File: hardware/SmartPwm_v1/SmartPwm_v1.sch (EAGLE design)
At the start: 41 parts, among them IC1 7805T, J1 ESP32-PICO-KIT, Q1 IRF3704-H, Q2 IRF3704-H, Q3 IRF3704-H, Q4 IRF3704-H, U1 ICL7667CBAZA, U3 ICL7667CBAZA

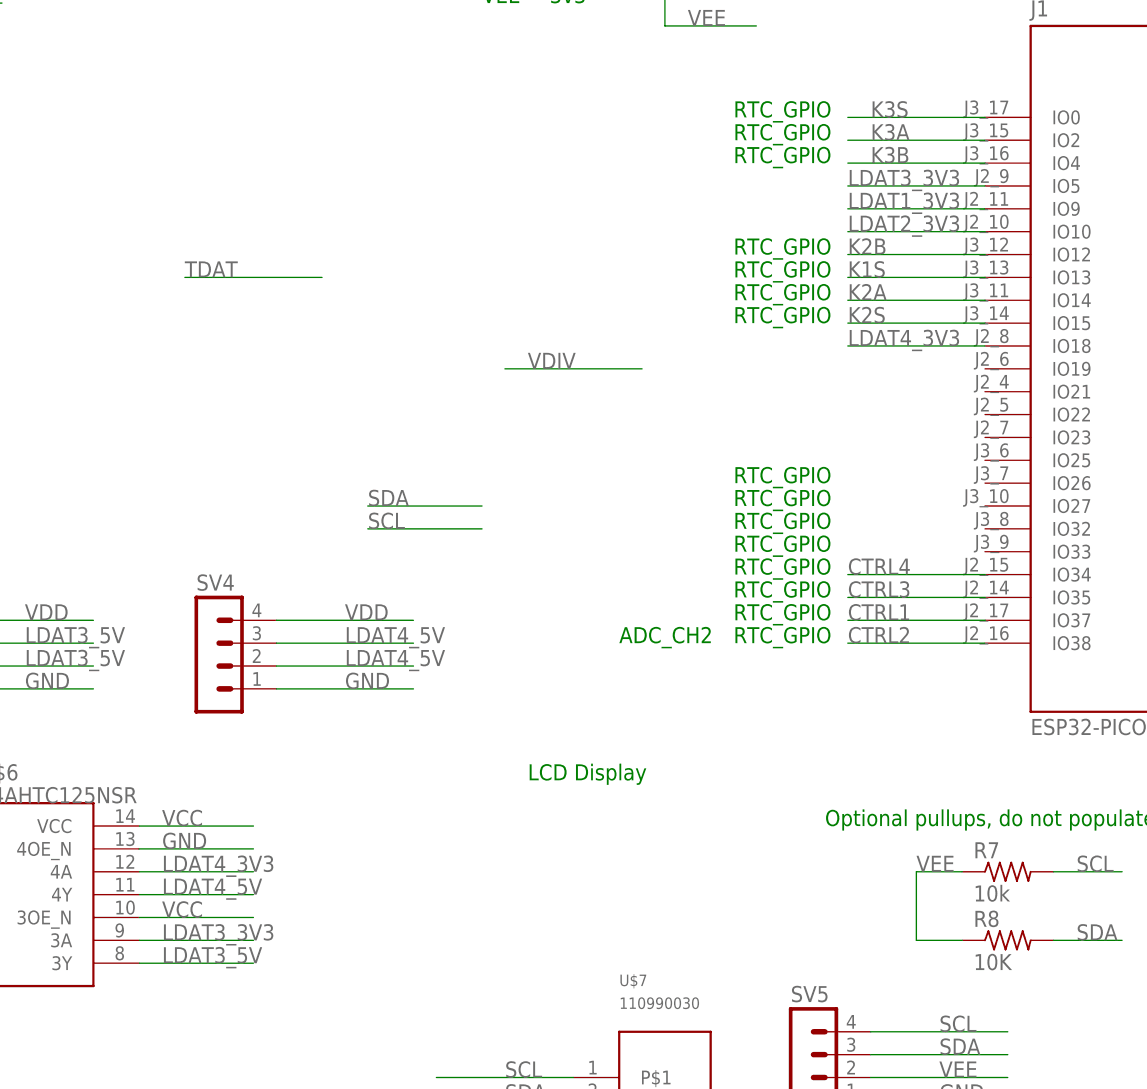
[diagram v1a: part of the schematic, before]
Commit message: did routing, but need to fix ctrl pins, since they were routed to inputs on the pico kit...
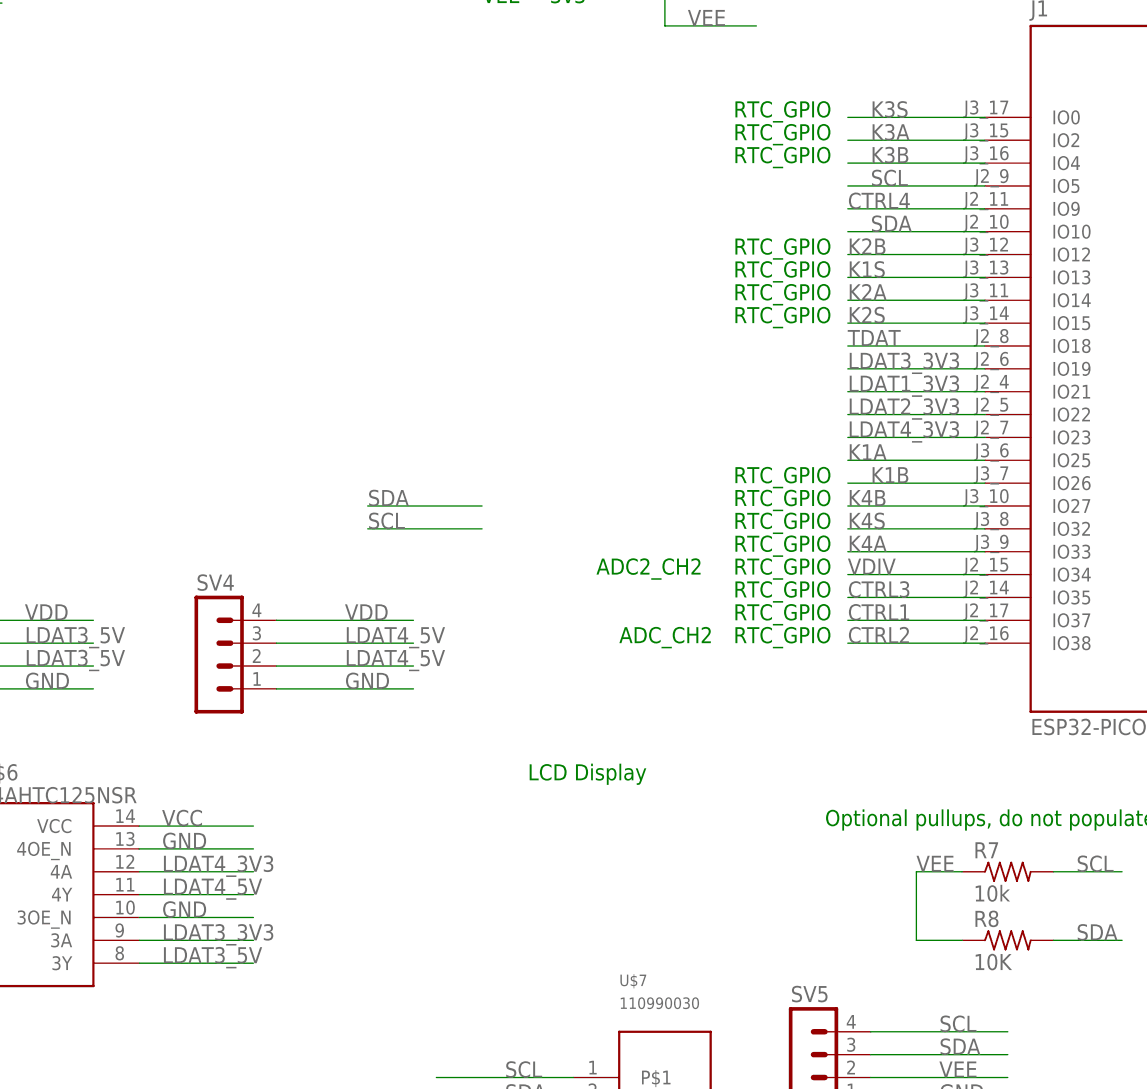
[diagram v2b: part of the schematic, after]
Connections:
- net CTRL4: now also J1.IO9; no longer J1.IO34
- net GND: now also U$6.3OE_N
- net K1A: now also J1.IO25
- net K1B: now also J1.IO26
- net K4A: now also J1.IO33
- net K4B: now also J1.IO27
- net K4S: now also J1.IO32
- net LDAT1_3V3: now also J1.IO21; no longer J1.IO9
- net LDAT2_3V3: now also J1.IO22; no longer J1.IO10
- net LDAT3_3V3: now also J1.IO19; no longer J1.IO5
- net LDAT4_3V3: now also J1.IO23; no longer J1.IO18
- net SCL: now also J1.IO5
- net SDA: now also J1.IO10
- net TDAT: now also J1.IO18
- net VCC: no longer U$6.3OE_N
- net VDIV: now also J1.IO34
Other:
- note added: "ADC2_CH2"
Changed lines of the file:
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@@
 <text x="228.6" y="-58.42" size="1.778" layer="91">tantalum</text>
 <text x="266.7" y="-58.42" size="1.778" layer="91">lowimpedance</text>
+<text x="7.62" y="-38.1" size="1.778" layer="91">ADC2_CH2</text>
 </plain>
 <instances>
@@
 <pinref part="SV4" gate="1" pin="1"/>
 </segment>
+<segment>
+<wire x1="-30.48" y1="-76.2" x2="-43.18" y2="-76.2" width="0.1524" layer="91"/>
+<label x="-40.64" y="-76.2" size="1.778" layer="95"/>
+<pinref part="U$6" gate="G$1" pin="3OE_N"/>
+</segment>
 </net>
 <net name="VCC" class="0">
@@
 <label x="-40.64" y="-66.04" size="1.778" layer="95"/>
 <pinref part="U$6" gate="G$1" pin="VCC"/>
-</segment>
-<segment>
-<wire x1="-30.48" y1="-76.2" x2="-43.18" y2="-76.2" width="0.1524" layer="91"/>
-<label x="-40.64" y="-76.2" size="1.778" layer="95"/>
-<pinref part="U$6" gate="G$1" pin="3OE_N"/>
 </segment>
 </net>
@@
 </segment>
 <segment>
-<wire x1="50.8" y1="-38.1" x2="35.56" y2="-38.1" width="0.1524" layer="91"/>
-<label x="35.56" y="-38.1" size="1.778" layer="95"/>
-<pinref part="J1" gate="G$1" pin="IO34"/>
+<wire x1="50.8" y1="2.54" x2="35.56" y2="2.54" width="0.1524" layer="91"/>
+<label x="35.56" y="2.54" size="1.778" layer="95"/>
+<pinref part="J1" gate="G$1" pin="IO9"/>
 </segment>
 </net>
@@
 <label x="-17.78" y="-33.02" size="1.778" layer="95"/>
 </segment>
+<segment>
+<wire x1="50.8" y1="5.08" x2="35.56" y2="5.08" width="0.1524" layer="91"/>
+<label x="38.1" y="5.08" size="1.778" layer="95"/>
+<pinref part="J1" gate="G$1" pin="IO5"/>
+</segment>
 </net>
 <net name="SDA" class="0">
@@
 <wire x1="-5.08" y1="-30.48" x2="-17.78" y2="-30.48" width="0.1524" layer="91"/>
 <label x="-17.78" y="-30.48" size="1.778" layer="95"/>
+</segment>
+<segment>
+<wire x1="50.8" y1="0" x2="35.56" y2="0" width="0.1524" layer="91"/>
+<label x="38.1" y="0" size="1.778" layer="95"/>
+<pinref part="J1" gate="G$1" pin="IO10"/>
 </segment>
 </net>
@@
 </segment>
 <segment>
-<wire x1="-22.86" y1="-5.08" x2="-38.1" y2="-5.08" width="0.1524" layer="91"/>
-<label x="-38.1" y="-5.08" size="1.778" layer="95"/>
+<wire x1="50.8" y1="-12.7" x2="35.56" y2="-12.7" width="0.1524" layer="91"/>
+<label x="35.56" y="-12.7" size="1.778" layer="95"/>
+<pinref part="J1" gate="G$1" pin="IO18"/>
 </segment>
 </net>
@@
 <label x="-71.12" y="104.14" size="1.778" layer="95"/>
 </segment>
+<segment>
+<wire x1="50.8" y1="-27.94" x2="35.56" y2="-27.94" width="0.1524" layer="91"/>
+<label x="38.1" y="-27.94" size="1.778" layer="95"/>
+<pinref part="J1" gate="G$1" pin="IO26"/>
+</segment>
 </net>
 <net name="K4S" class="0">
@@
 <pinref part="MT4" gate="G$1" pin="2"/>
 </segment>
+<segment>
+<wire x1="50.8" y1="-33.02" x2="35.56" y2="-33.02" width="0.1524" layer="91"/>
+<label x="35.56" y="-33.02" size="1.778" layer="95"/>
+<pinref part="J1" gate="G$1" pin="IO32"/>
+</segment>
 </net>
 <net name="K4A" class="0">
@@
 <pinref part="MT4" gate="G$1" pin="A"/>
 </segment>
+<segment>
+<pinref part="J1" gate="G$1" pin="IO33"/>
+<wire x1="50.8" y1="-35.56" x2="35.56" y2="-35.56" width="0.1524" layer="91"/>
+<label x="35.56" y="-35.56" size="1.778" layer="95"/>
+</segment>
 </net>
 <net name="K4B" class="0">
@@
 <label x="-71.12" y="25.4" size="1.778" layer="95"/>
 <pinref part="MT4" gate="G$1" pin="B"/>
+</segment>
+<segment>
+<wire x1="50.8" y1="-30.48" x2="35.56" y2="-30.48" width="0.1524" layer="91"/>
+<label x="35.56" y="-30.48" size="1.778" layer="95"/>
+<pinref part="J1" gate="G$1" pin="IO27"/>
 </segment>
 </net>
@@
 </segment>
 <segment>
-<wire x1="12.7" y1="-15.24" x2="-2.54" y2="-15.24" width="0.1524" layer="91"/>
-<label x="0" y="-15.24" size="1.778" layer="95"/>
+<wire x1="50.8" y1="-38.1" x2="35.56" y2="-38.1" width="0.1524" layer="91"/>
+<label x="35.56" y="-38.1" size="1.778" layer="95"/>
+<pinref part="J1" gate="G$1" pin="IO34"/>
 </segment>
 </net>
@@
 </segment>
 <segment>
-<wire x1="50.8" y1="2.54" x2="35.56" y2="2.54" width="0.1524" layer="91"/>
-<label x="35.56" y="2.54" size="1.778" layer="95"/>
-<pinref part="J1" gate="G$1" pin="IO9"/>
+<wire x1="50.8" y1="-17.78" x2="35.56" y2="-17.78" width="0.1524" layer="91"/>
+<label x="35.56" y="-17.78" size="1.778" layer="95"/>
+<pinref part="J1" gate="G$1" pin="IO21"/>
 </segment>
 </net>
@@
 </segment>
 <segment>
-<wire x1="50.8" y1="0" x2="35.56" y2="0" width="0.1524" layer="91"/>
-<label x="35.56" y="0" size="1.778" layer="95"/>
-<pinref part="J1" gate="G$1" pin="IO10"/>
+<wire x1="50.8" y1="-20.32" x2="35.56" y2="-20.32" width="0.1524" layer="91"/>
+<label x="35.56" y="-20.32" size="1.778" layer="95"/>
+<pinref part="J1" gate="G$1" pin="IO22"/>
 </segment>
 </net>
@@
 </segment>
 <segment>
-<wire x1="50.8" y1="-12.7" x2="35.56" y2="-12.7" width="0.1524" layer="91"/>
-<label x="35.56" y="-12.7" size="1.778" layer="95"/>
-<pinref part="J1" gate="G$1" pin="IO18"/>
+<wire x1="50.8" y1="-22.86" x2="35.56" y2="-22.86" width="0.1524" layer="91"/>
+<label x="35.56" y="-22.86" size="1.778" layer="95"/>
+<pinref part="J1" gate="G$1" pin="IO23"/>
 </segment>
 </net>
@@
 </segment>
 <segment>
-<wire x1="50.8" y1="5.08" x2="35.56" y2="5.08" width="0.1524" layer="91"/>
-<label x="35.56" y="5.08" size="1.778" layer="95"/>
-<pinref part="J1" gate="G$1" pin="IO5"/>
+<wire x1="50.8" y1="-15.24" x2="35.56" y2="-15.24" width="0.1524" layer="91"/>
+<label x="35.56" y="-15.24" size="1.778" layer="95"/>
+<pinref part="J1" gate="G$1" pin="IO19"/>
 </segment>
 </net>
@@
 <label x="-71.12" y="106.68" size="1.778" layer="95"/>
 </segment>
+<segment>
+<wire x1="50.8" y1="-25.4" x2="35.56" y2="-25.4" width="0.1524" layer="91"/>
+<label x="35.56" y="-25.4" size="1.778" layer="95"/>
+<pinref part="J1" gate="G$1" pin="IO25"/>
+</segment>
 </net>
 <net name="K3S" class="0">
@@
 </sheet>
 </sheets>
+<errors>
+</errors>
 </schematic>
 </drawing>

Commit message: begin schematic for nano BLE sense based pwm module
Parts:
- removed C10: AVX_TPSA475K020R1800AVX_TPSA475K020R1800_0_0, AVX - TPSA475K020R1800:AVX_TPSA475K020R1800AVX_TPSA475K020R1800_0_0
- removed C12, C4: .1uf, rcl:C-USC0805
- removed C3: .33uf, rcl:C-USC0805
- removed C5, C8: 10uf, rcl:C-USC0805
- removed IC1: 7805T, linear:7805T
- removed J1: ESP32-PICO-KIT, ESP32-PICO-KIT:ESP32-PICO-KIT
- removed MT3, MT4: PEC11R-4215F-S0024, PEC11R-4215F-S0024:PEC11R-4215F-S0024
- removed Q3, Q4: IRF3704-H, transistor-power:IRF3704-H
- removed R6, R8: 10K, rcl:R-US_R0805
- removed R7: 10k, rcl:R-US_R0805
- removed SV1, SV2, SV3, SV4, SV5: (no value), con-lstb:MA04-1
- removed U$3, U$4: TB002-500-P02, mylib:TB002-500-P02
- removed U$6: 74AHTC125NSR, DIP794W45P254L1969H508Q14:74AHTC125NSR
- removed U$7: 110990030, seeedgrove:110990030
- removed U1: ICL7667CBAZA, ICL7667CBAZA:ICL7667CBAZA
- added C2: 10uf, rcl:C-USC0805
- added LED1, LED2, LED3: TLLR4400, led:TLLR4400
- added M1: ARDUINO-NANO-3.0, diy-modules:ARDUINO-NANO-3.0
- added R1, R2, R3: 220, rcl:R-US_R0805
- U$5: value TEMP-HUM-SENSOR-DHT11 -> TB002-500-P02; device diy-modules:TEMP-HUM-SENSOR-DHT11 -> mylib:TB002-500-P02
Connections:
- removed net GATE3: Q3.G, U1.OUT_A
- removed net GATE4: Q4.G, U1.OUT_B
- removed net K3A: J1.IO2, MT3.A
- removed net K3B: J1.IO4, MT3.B
- removed net K3S: J1.IO0, MT3.2
- removed net K4A: J1.IO33, MT4.A
- removed net K4B: J1.IO27, MT4.B
- removed net K4S: J1.IO32, MT4.2
- removed net LDAT1_3V3: J1.IO21, U$6.1A
- removed net LDAT1_5V: SV1.2, SV1.3, U$6.1Y
- removed net LDAT2_3V3: J1.IO22, U$6.2A
- removed net LDAT2_5V: SV2.2, SV2.3, U$6.2Y
- removed net LDAT3_3V3: J1.IO19, U$6.3A
- removed net LDAT3_5V: SV3.2, SV3.3, U$6.3Y
- removed net LDAT4_3V3: J1.IO23, U$6.4A
- removed net LDAT4_5V: SV4.2, SV4.3, U$6.4Y
- removed net LOAD_RET3: C8.2, Q3.D, U$3.P$2
- removed net LOAD_RET4: C5.2, Q4.D, U$4.P$2
- removed net SCL: J1.IO5, R7.2, SV5.4, U$7.P$1
- removed net SDA: J1.IO10, R8.2, SV5.3, U$7.P$2
- removed net TDAT: J1.IO18, R6.2, U$5.DAT
- new net D1_N: LED1.C, M1.D1/TX
- new net D2_N: LED2.C, M1.D0/RX
- new net D3_N: LED3.C, M1.D12/MISO
- new net N$1: LED1.A, R1.1
- new net N$2: LED2.A, R2.1
- new net N$3: LED3.A, R3.1
- net CTRL1: now also M1.D9; no longer J1.IO37
- net CTRL2: now also M1.D10; no longer J1.IO38
- net CTRL3: now also M1.D11/MOSI; no longer J1.IO35, U1.IN_A
- net CTRL4: now also M1.D3; no longer J1.IO9, U1.IN_B
- net GND: now also C2.2, M1.GND.1, M1.GND.2, U$5.P$2; no longer C10.CATHODE, C12.2, C3.2, C4.2, IC1.GND, J1.GND_1, J1.GND_2, MT3.1, MT3.COM, MT3.SHIELD, MT4.1, MT4.COM, MT4.SHIELD, Q3.S, Q4.S, SV1.1, SV2.1, SV3.1, SV4.1, SV5.1, U$5.GND, U$6.1OE_N, U$6.2OE_N, U$6.3OE_N, U$6.4OE_N, U$6.GND, U$7.P$4, U1.V-
- net K1A: now also M1.D4; no longer J1.IO25
- net K1B: now also M1.D5; no longer J1.IO26
- net K1S: now also M1.D6; no longer J1.IO13
- net K2A: now also M1.D7; no longer J1.IO14
- net K2B: now also M1.D8; no longer J1.IO12
- net K2S: now also M1.D2; no longer J1.IO15
- net VCC: now also M1.5V; no longer C4.1, IC1.VO, J1.EXT_5V, U$6.VCC
- net VDD: now also C2.1, M1.VIN, U$5.P$1; no longer C10.ANODE, C12.1, C3.1, C5.1, C8.1, IC1.VI, SV1.4, SV2.4, SV3.4, SV4.4, U$3.P$1, U$4.P$1, U1.V+
- net VDIV: now also M1.A0; no longer J1.IO34
- net VEE: now also M1.3V3, R1.2, R2.2, R3.2; no longer J1.VDD33_1, J1.VDD33_2, R6.1, R7.1, R8.1, SV5.2, U$5.VDD, U$7.P$3
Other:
- note added: "Led's"
- note removed: "ADC2_CH2"
- note removed: "ADC_CH2"
- note removed: "LCD Display"
- note removed: "Optional pullups, do not populate if not needed"
- note removed: "Optional, connector if desired to go grove to grove. beware of orintation during install"
- note removed: "Power Regulator"
- note removed: "RTC_GPIO"
- note removed: "Temperature"
- note removed: "ws2815"
- moved on the sheet: C1, C11, C6, C7, C9, MT1, MT2, Q1, Q2, R10, R9, U3

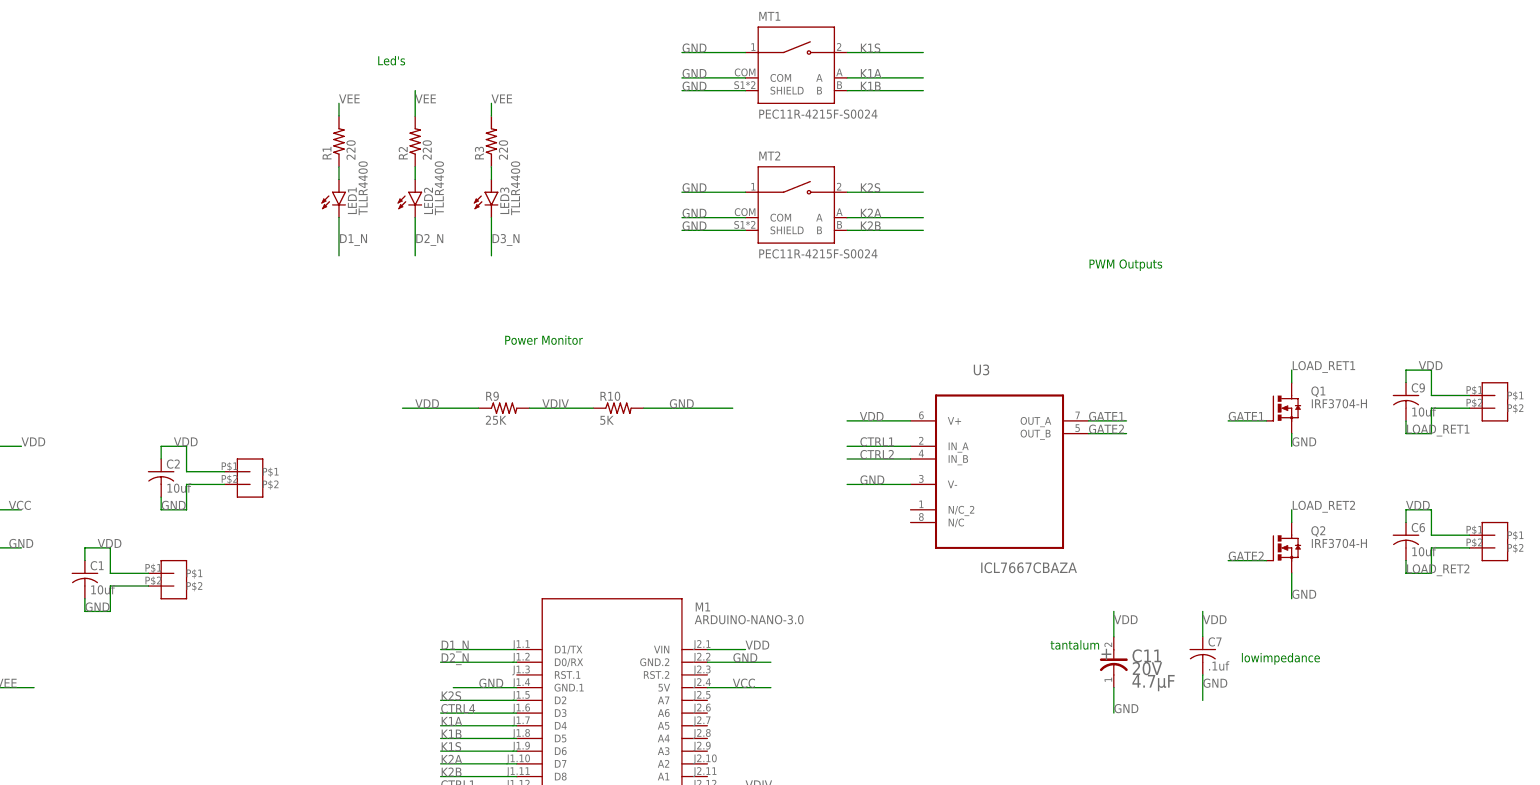
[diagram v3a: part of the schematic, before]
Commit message: back to through hole design...
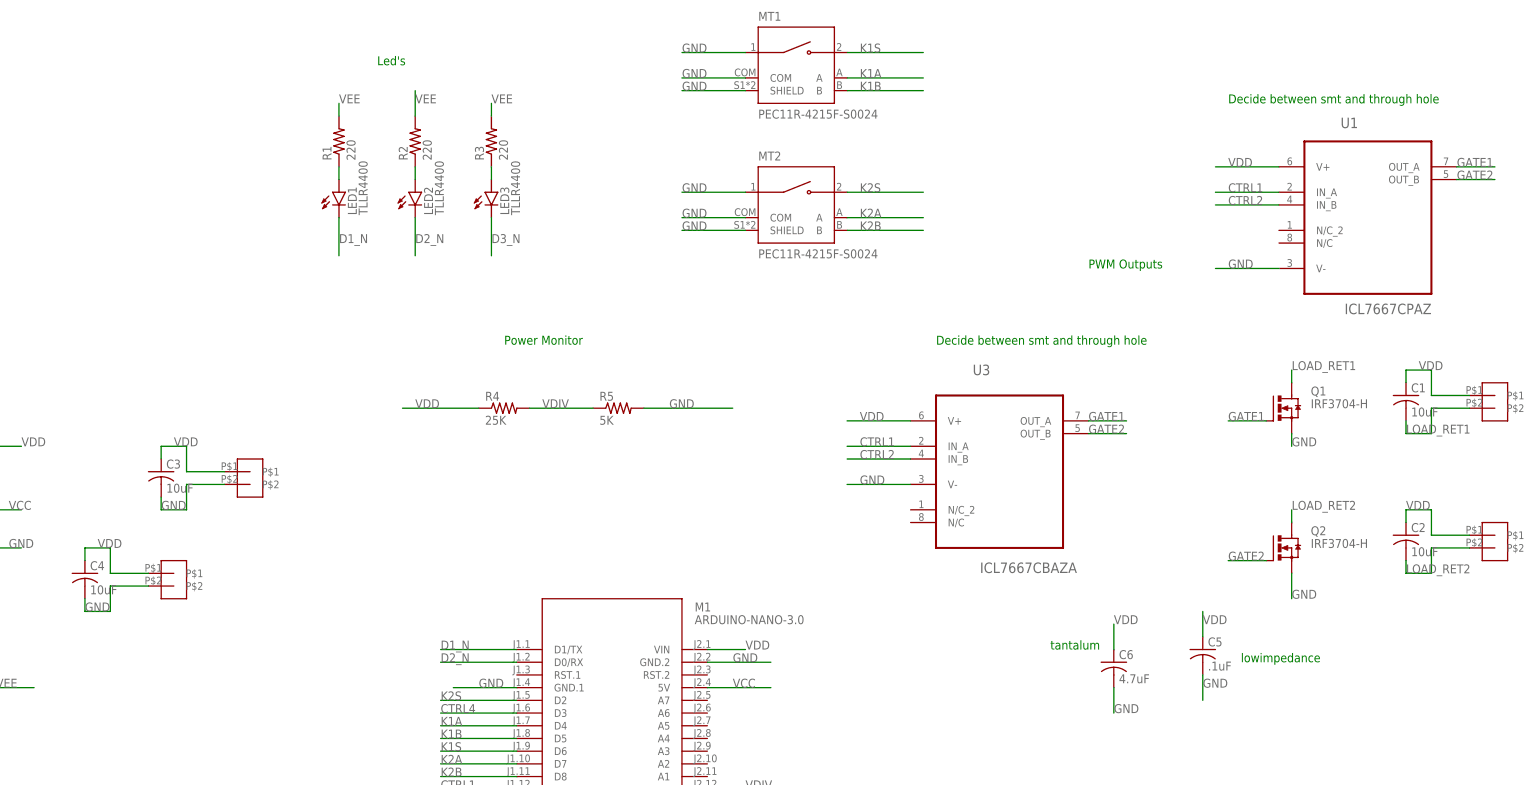
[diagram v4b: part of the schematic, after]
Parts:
- removed C11: AVX_TPSA475K020R1800AVX_TPSA475K020R1800_0_0, AVX - TPSA475K020R1800:AVX_TPSA475K020R1800AVX_TPSA475K020R1800_0_0
- removed C7: .1uf, rcl:C-USC0805
- removed C9: 10uf, rcl:C-USC0805
- removed R10: 5K, rcl:R-US_R0805
- removed R9: 25K, rcl:R-US_R0805
- added C3, C4: 10uF, rcl:C-US025-024X044
- added C5: .1uF, rcl:C-US025-024X044
- added R4: 25K, rcl:R-US_0207/10
- added R5: 5K, rcl:R-US_0207/10
- added U1: ICL7667CPAZ, ICL7667CPAZ:ICL7667CPAZ
- C1, C2: value 10uf -> 10uF; device rcl:C-USC0805 -> rcl:C-US025-024X044
- C6: value 10uf -> 4.7uF; device rcl:C-USC0805 -> rcl:C-US025-024X044
- R1, R2, R3: device rcl:R-US_R0805 -> rcl:R-US_0207/10
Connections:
- net CTRL1: now also U1.IN_A
- net CTRL2: now also U1.IN_B
- net GATE1: now also U1.OUT_A
- net GATE2: now also U1.OUT_B
- net GND: now also C3.2, C4.2, C5.2, C6.2, R5.2, U1.V-; no longer C1.2, C11.CATHODE, C2.2, C7.2, R10.2
- net LOAD_RET1: now also C1.2; no longer C9.2
- net LOAD_RET2: now also C2.2; no longer C6.2
- net VDD: now also C3.1, C4.1, C5.1, R4.1, U1.V+; no longer C11.ANODE, C7.1, C9.1, R9.1
- net VDIV: now also R4.2, R5.1; no longer R10.1, R9.2
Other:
- note added: "Decide between smt and through hole"
- moved on the sheet: C1, C2, C6
